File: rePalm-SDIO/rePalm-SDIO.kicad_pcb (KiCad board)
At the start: 2 copper layers, 50 x 24 mm, 18 parts, among them J1 SD Connector, J2 SWD, J3 BootRST, U1 STM32H7B0RBT6, U2 S25FL064LABMFN010, U3 APS6404L-3SQR-SN, U4 LTC3406BES5-1.2

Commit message: Finished initial layout and board
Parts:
- U2, U3: footprint Package_SO:SOIC-8_5.275x5.275mm_P1.27mm -> stm32:BACKWARDS-SOIC-8_5.275x5.275mm_P1.27mm
- moved C1_2 3.24 mm to (125.2, 117.5)
- moved C4_2 2.23 mm to (122.7, 116.5), turned to -90 degrees
- moved U1 2.05 mm to (129.3, 125.5)
- moved C1_4 1.65 mm to (132.3, 117.2)
- moved C4_1 1.10 mm to (119.5, 119.2), turned to 180 degrees
- moved U4 1.07 mm to (119.6, 116.5)
- moved C1_3 1.02 mm to (133.4, 132.8)
- turned C2 to 0 degrees
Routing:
- net Net-(C1_4-Pad2): track 0.00 -> 151.3 mm, vias 0 -> 5
- net Net-(C1_1-Pad2): track 0.00 -> 111.6 mm, vias 0 -> 4
- net Net-(U1-Pad50): track 0.00 -> 45.5 mm, vias 0 -> 4
- net Net-(J2-Pad1): track 0.00 -> 40.7 mm, vias 0 -> 1
- net Net-(J2-Pad2): track 0.00 -> 40.6 mm, vias 0 -> 1
- net Net-(U1-Pad26): track 0.00 -> 33.4 mm, vias 0 -> 2
- net Net-(J3-Pad1): track 0.00 -> 32.4 mm, vias 0 -> 2
- net Net-(U1-Pad29): track 0.00 -> 27.9 mm, vias 0 -> 2
- net Net-(U1-Pad57): track 0.00 -> 26.3 mm, vias 0 -> 2
- net Net-(U1-Pad23): track 0.00 -> 24.6 mm, vias 0 -> 2
- net Net-(J3-Pad2): track 0.00 -> 24.3 mm, vias 0 -> 1
- net Net-(U1-Pad55): track 0.00 -> 20.8 mm, vias 0 -> 2
- net Net-(R1-Pad2): track 0.00 -> 18.5 mm, vias 0 -> 2
- net Net-(U1-Pad28): track 0.00 -> 18.1 mm, vias 0 -> 2
- net Net-(U1-Pad27): track 0.00 -> 17.0 mm, vias 0 -> 2
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- added copper zone on F.Cu, net Net-(C1_4-Pad2)
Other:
- outline, holes or cut-outs redrawn
- board text added: "1"
- board text added: "Both SOIC8 chips to be installed upside down"

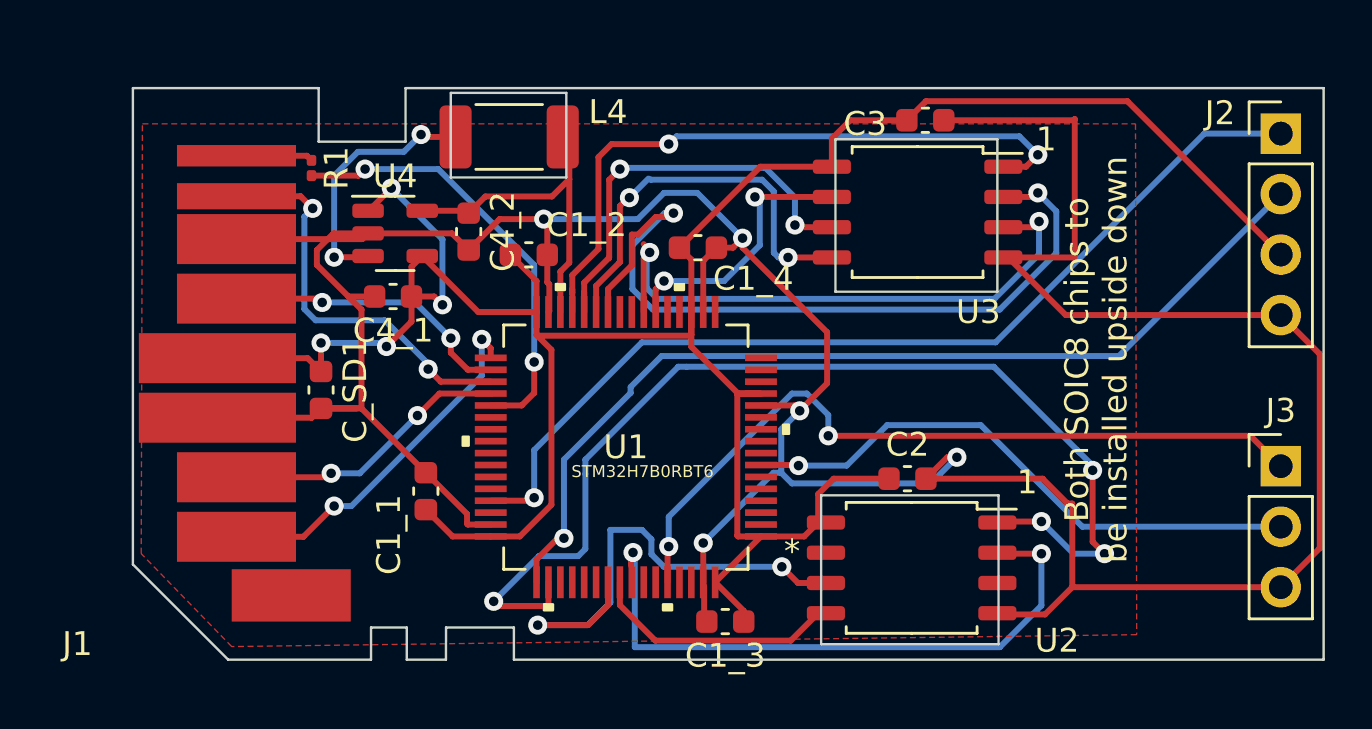
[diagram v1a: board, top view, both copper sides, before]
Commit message: Minor layout changes
Added two new layers for power&ground planes, added SD breakout for debugging, re-jigged SD connector
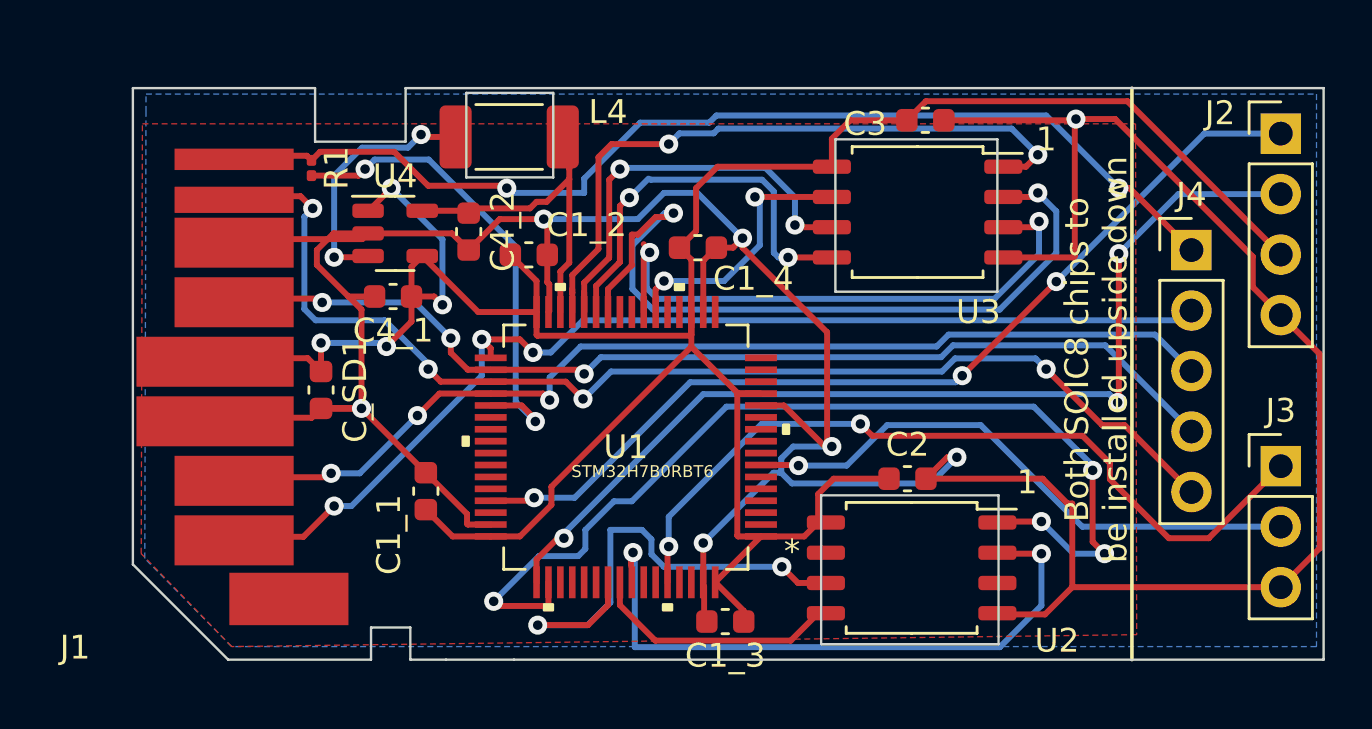
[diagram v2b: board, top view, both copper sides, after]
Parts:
- added J4: Conn_01x05, Connector_PinHeader_2.54mm:PinHeader_1x05_P2.54mm_Vertical, F.Cu at (153.0, 117.2)
- moved J1 0.18 mm to (108.7, 134.4)
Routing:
- net Net-(J1-Pad8): track 3.23 -> 45.1 mm, vias 0 -> 2
- net Net-(J1-Pad7): track 17.0 -> 49.8 mm, vias 2 -> 4
- net Net-(J1-Pad5): track 12.3 -> 44.1 mm, vias 2 -> 3
- net Net-(J1-Pad2): track 12.2 -> 44.0 mm, vias 2 -> 3
- net Net-(J1-Pad1): track 15.6 -> 46.4 mm, vias 2 -> 3
- net Net-(C1_1-Pad1): track 151.3 -> 154.7 mm, vias 5 -> 7
- net Net-(U1-Pad50): track 45.5 -> 42.4 mm
- net Net-(C1_1-Pad2): track 111.6 -> 114.3 mm
- net Net-(J2-Pad2): track 40.6 -> 42.7 mm, vias 1 -> 3
- net Net-(R1-Pad2): track 18.5 -> 20.3 mm
- net Net-(J3-Pad1): track 32.4 -> 33.7 mm
- net Net-(J2-Pad1): track 40.7 -> 39.6 mm, vias 1 -> 3
- net Net-(C4_2-Pad1): track 14.3 -> 15.3 mm
- added copper zone on B.Cu, net Net-(C1_1-Pad1)
- added copper zone on In1.Cu, net Net-(C1_1-Pad1)
- added copper zone on In2.Cu, net Net-(C1_1-Pad2)
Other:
- outline, holes or cut-outs redrawn
- copper layers 2 -> 4

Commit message: Flipped STM and re-routed
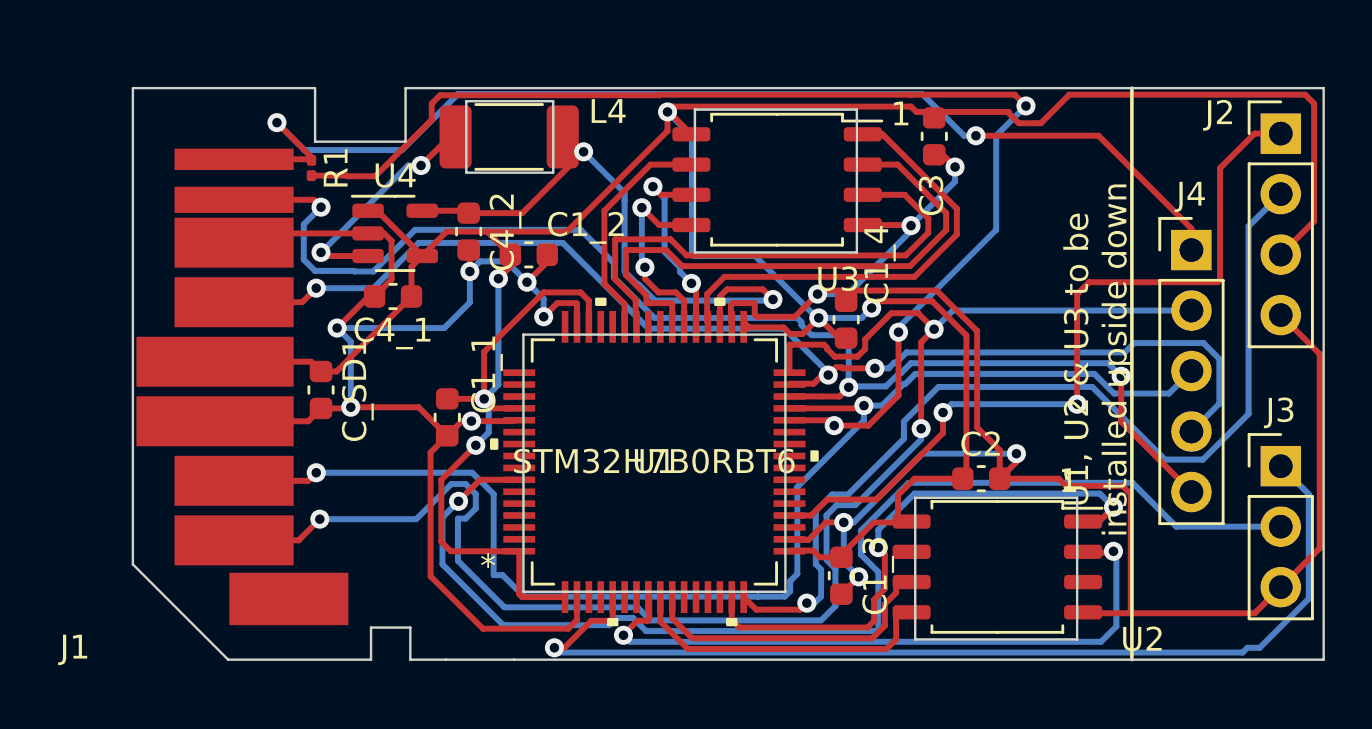
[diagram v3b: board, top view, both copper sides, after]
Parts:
- U1: footprint LQFP_B0VBT6_STM:STM32H7B0RBT6 -> LQFP_B0VBT6_STM:STM32H7B0RBT6_UpsideDown
- moved C1_4 6.92 mm to (138.5, 120.2), turned to 90 degrees
- moved U3 6.05 mm to (135.6, 114.3)
- moved C1_3 5.24 mm to (138.3, 130.9), turned to -90 degrees
- moved U2 3.60 mm to (144.8, 130.6)
- moved C1_1 3.23 mm to (121.8, 124.3), turned to 90 degrees
- moved C2 3.10 mm to (144.2, 126.8)
- moved U1 1.35 mm to (130.4, 126.1)
- moved C3 0.77 mm to (142.2, 112.5), turned to -90 degrees
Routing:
- net Net-(R1-Pad2): track 20.3 -> 51.6 mm, vias 2 -> 3
- net Net-(J3-Pad2): track 24.3 -> 49.3 mm
- net Net-(C1_1-Pad2): track 114.3 -> 138.5 mm, vias 4 -> 6
- net Net-(J1-Pad1): track 46.4 -> 65.7 mm
- net Net-(U1-Pad50): track 42.4 -> 24.2 mm, vias 4 -> 2
- net Net-(C1_1-Pad1): track 154.7 -> 140.3 mm, vias 7 -> 12
- net Net-(J1-Pad2): track 44.0 -> 55.0 mm, vias 3 -> 2
- net Net-(U1-Pad28): track 18.1 -> 8.39 mm
- net Net-(U1-Pad26): track 33.4 -> 23.9 mm, vias 2 -> 0
- net Net-(U1-Pad29): track 28.2 -> 19.0 mm, vias 2 -> 0
- net Net-(C4_2-Pad1): track 15.3 -> 24.2 mm, vias 0 -> 2
- net Net-(J3-Pad1): track 33.7 -> 42.6 mm, vias 2 -> 1
- net Net-(U1-Pad27): track 17.0 -> 8.59 mm
- net Net-(U1-Pad55): track 20.8 -> 12.4 mm, vias 2 -> 0
- net Net-(J1-Pad5): track 44.1 -> 51.0 mm
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- removed copper zone on B.Cu, net Net-(C1_1-Pad1)
- removed copper zone on F.Cu, net Net-(C1_1-Pad1)
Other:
- outline, holes or cut-outs redrawn
- board text added: "U1, U2 & U3 to be installed upside down"
- board text removed: "Both SOIC8 chips to be installed upside down"

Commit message: Adjusted SD card connector
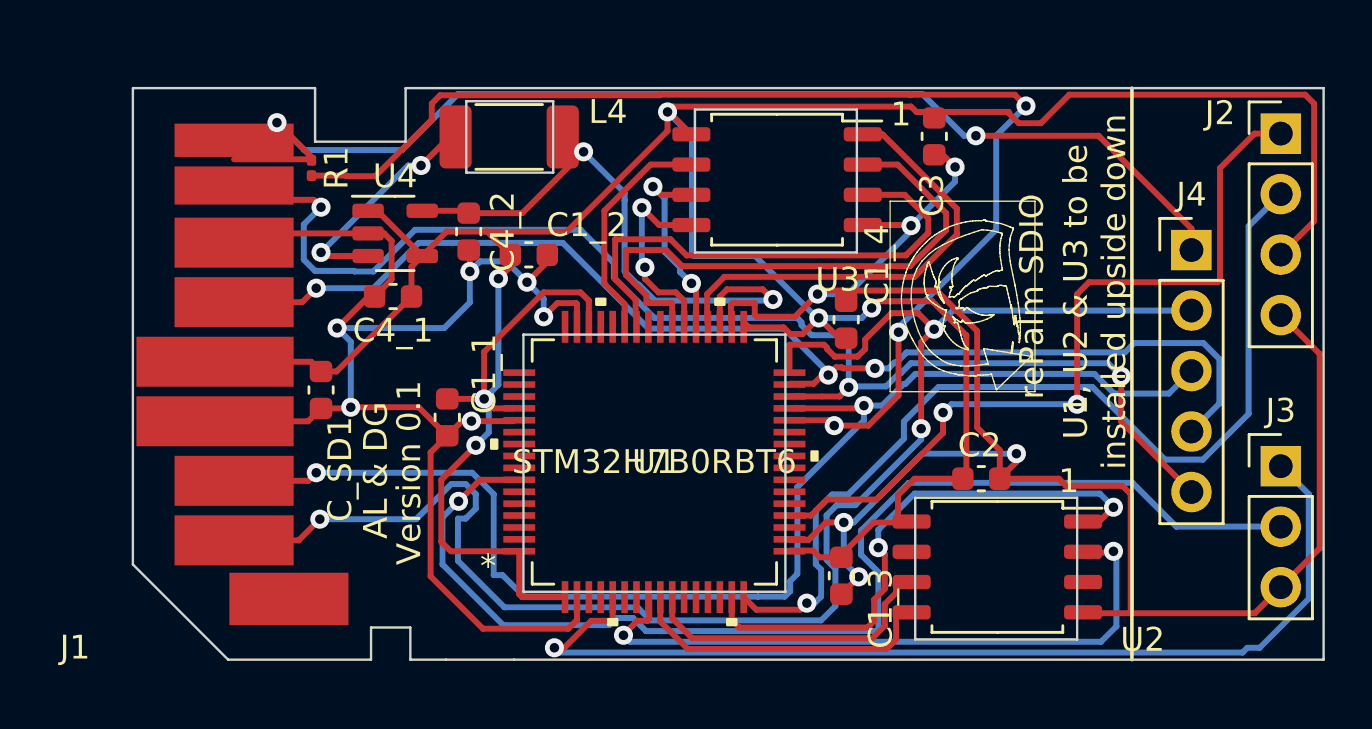
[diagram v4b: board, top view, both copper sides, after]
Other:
- board text added: "AL & DG"
- board text added: "Version 0.1"
- board text added: "rePalm SDIO"
